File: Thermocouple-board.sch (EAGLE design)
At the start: 69 parts, among them J1 RJ45, J11 1X2-3.5MM, J12 1X2-3.5MM, J13 1X2-3.5MM, J14 1X2-3.5MM, J2 RJ45, J3 1981584-1, SW1 PUSHBUTTON, SW2 PUSHBUTTON, U1 STM32F030K6, U10 MAX31855, U11 MAX31855, U12 MAX31855, U13 MAX31855, U20 EEPROM-I2C, U21 EEPROM-I2C, U30 ST3485, U40 LP298XS

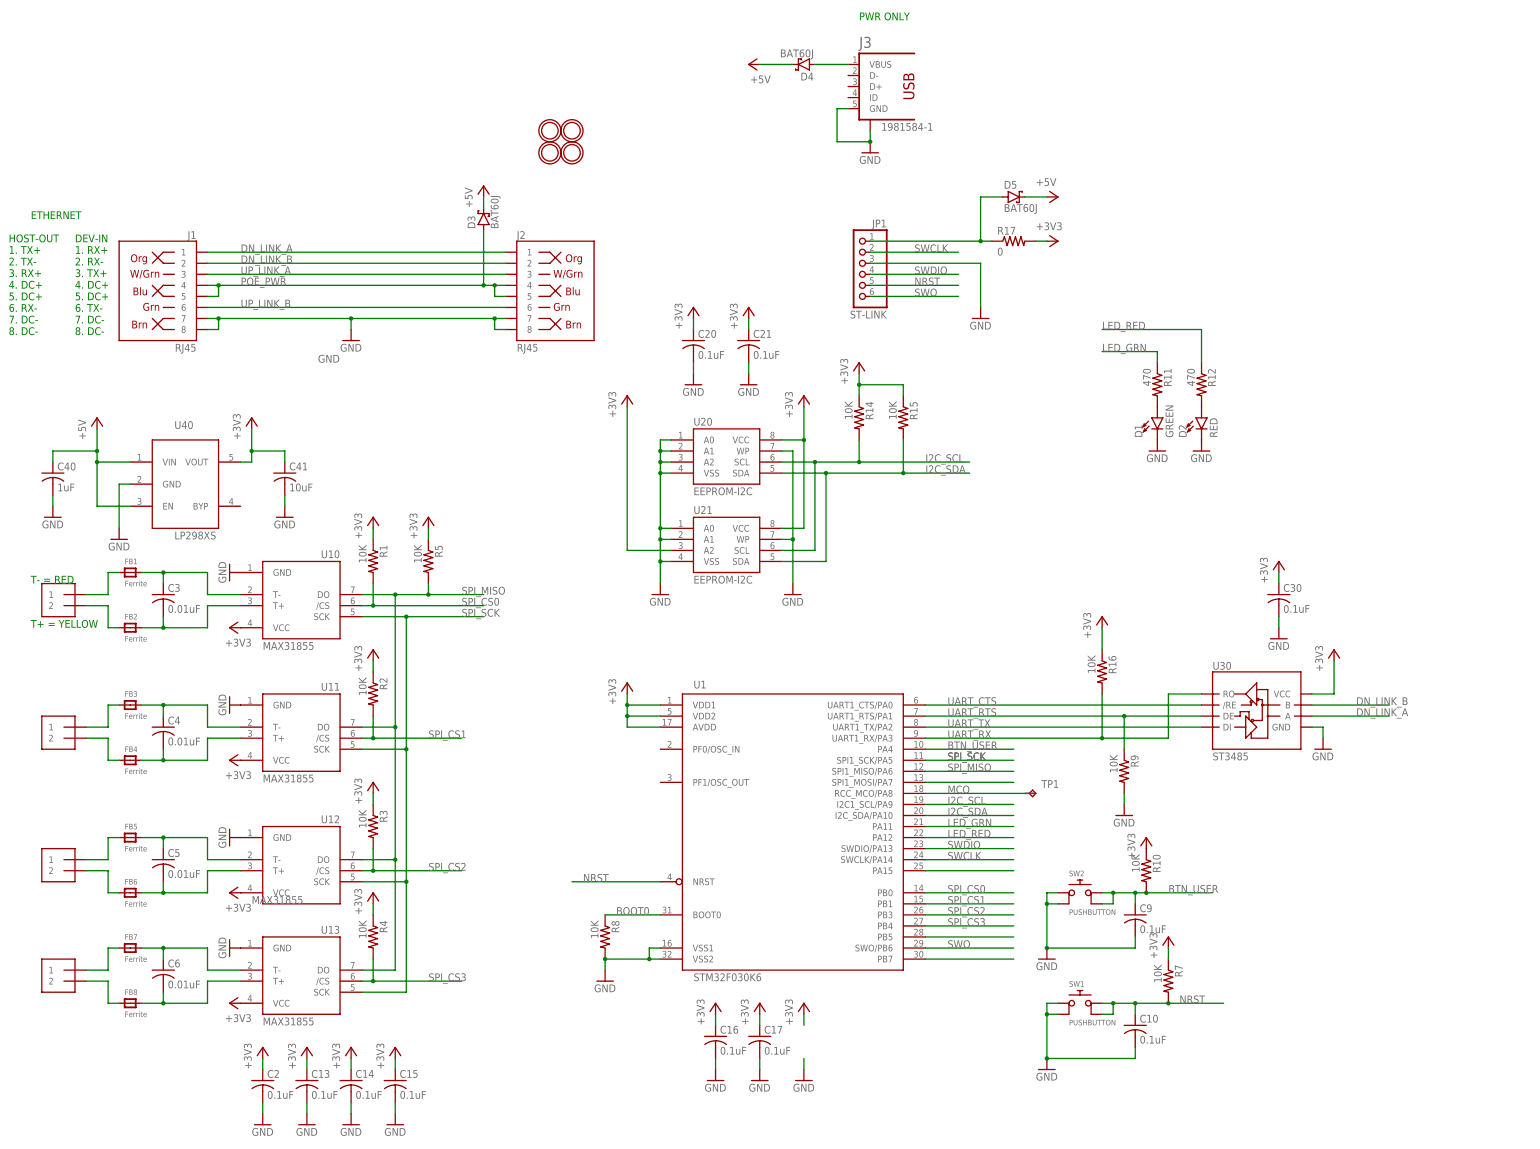
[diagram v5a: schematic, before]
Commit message: Start of move to STM32F042K4 with USB
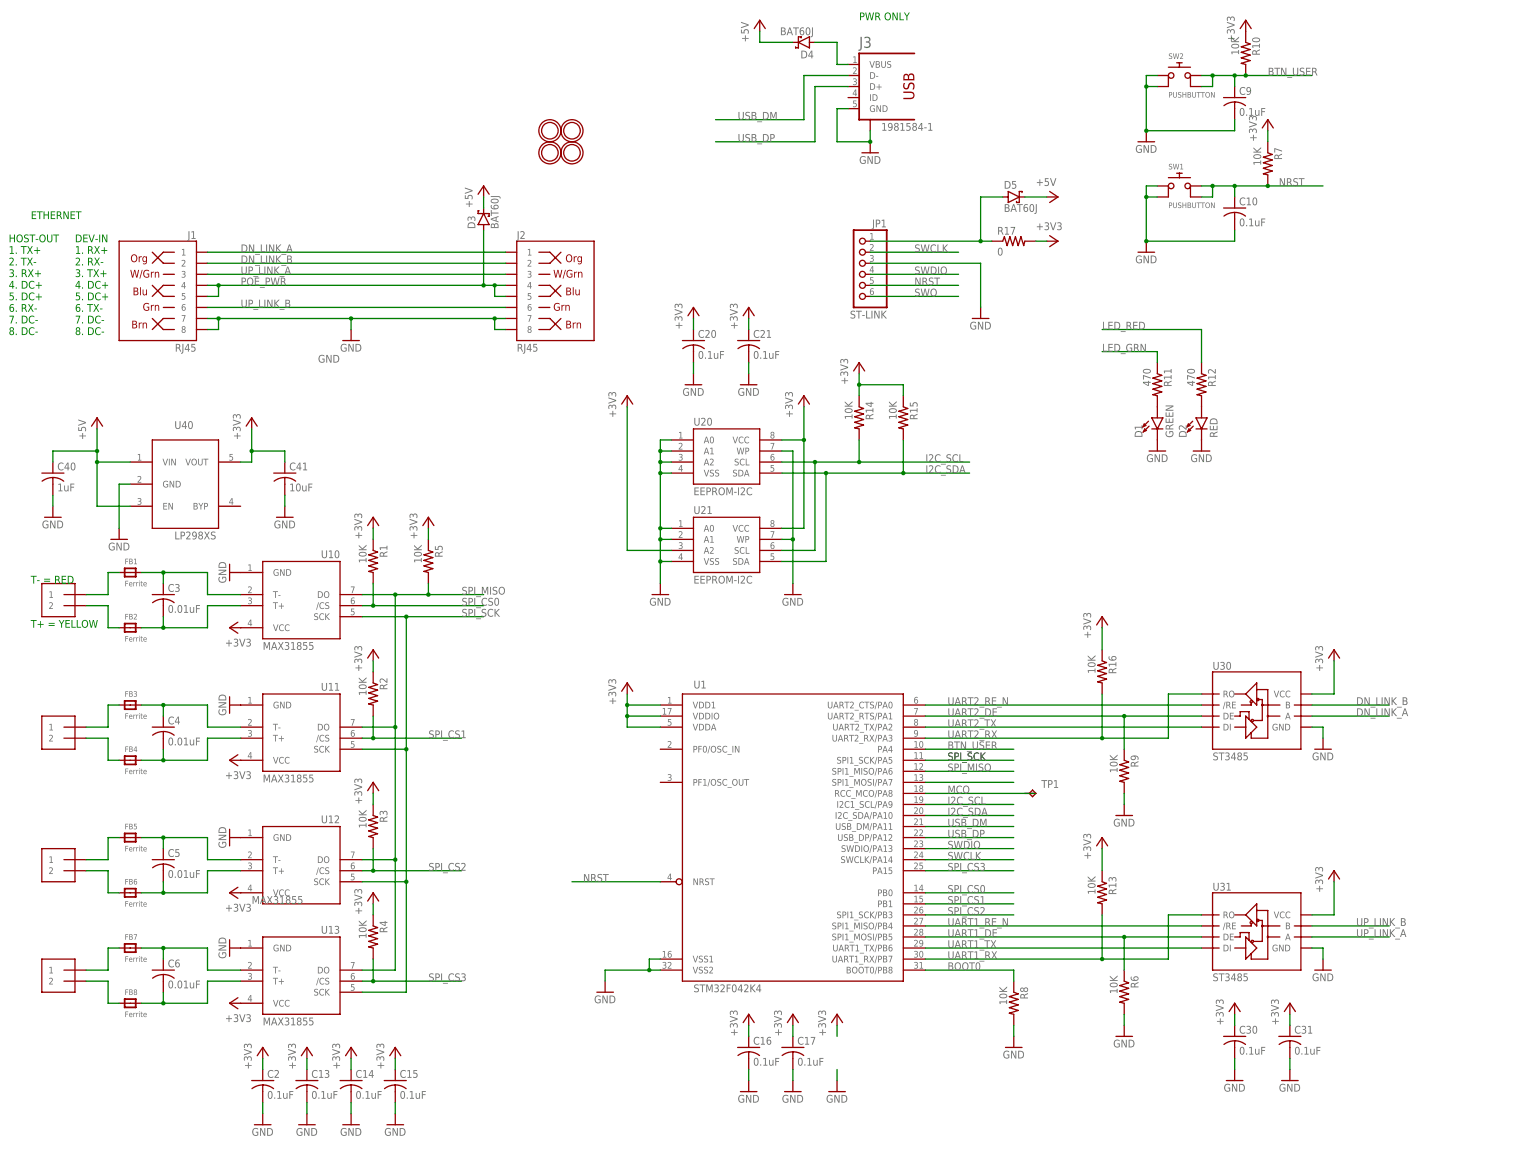
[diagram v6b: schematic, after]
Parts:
- added C31: 0.1uF, adafruit:C-USC0805K
- added R13, R6: 10K, adafruit:R-US_R0805
- added U31: ST3485, SparkFun-IC-Comms:RS485SOIC
- U1: value STM32F030K6 -> STM32F042K4; device Thermocouple-board:STM32F030K6_V01 -> Thermocouple-board:STM32F042K4_V01
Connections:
- removed net N$31: U1.PB5
- removed net N$35: U1.PB7
- removed net N$36: U1.PA15
- removed net UART_CTS: U1.UART1_CTS/PA0, U30./RE
- removed net UART_RTS: R9.1, U1.UART1_RTS/PA1, U30.DE
- removed net UART_RX: R16.2, U1.UART1_RX/PA3, U30.RO
- removed net UART_TX: U1.UART1_TX/PA2, U30.DI
- new net UART1_DE: R6.1, U1.SPI1_MOSI/PB5, U31.DE
- new net UART1_RE_N: U1.SPI1_MISO/PB4, U31./RE
- new net UART1_RX: R13.2, U1.UART1_RX/PB7, U31.RO
- new net UART1_TX: U1.UART1_TX/PB6, U31.DI
- new net UART2_DE: R9.1, U1.UART2_RTS/PA1, U30.DE
- new net UART2_RE_N: U1.UART2_CTS/PA0, U30./RE
- new net UART2_RX: R16.2, U1.UART2_RX/PA3, U30.RO
- new net UART2_TX: U1.UART2_TX/PA2, U30.DI
- new net USB_DM: J3.D-, U1.USB_DM/PA11
- new net USB_DP: J3.D+, U1.USB_DP/PA12
- net +3V3: now also C31.1, R13.1, U1.VDDA, U1.VDDIO, U31.VCC; no longer U1.AVDD, U1.VDD2
- net BOOT0: now also U1.BOOT0/PB8; no longer U1.BOOT0
- net GND: now also C31.2, R6.2, U31.GND
- net LED_GRN: no longer U1.PA11
- net LED_RED: no longer U1.PA12
- net SPI_CS2: now also U1.SPI1_SCK/PB3; no longer U1.PB3
- net SPI_CS3: now also U1.PA15; no longer U1.PB4
- net SWO: no longer U1.SWO/PB6
- net UP_LINK_A: now also U31.A
- net UP_LINK_B: now also U31.B
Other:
- moved on the sheet: C10, C16, C17, C30, C9, D4, R10, R7, R8, SW1, SW2, U1

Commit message: Ripup and start rerouting with USB and Xtal
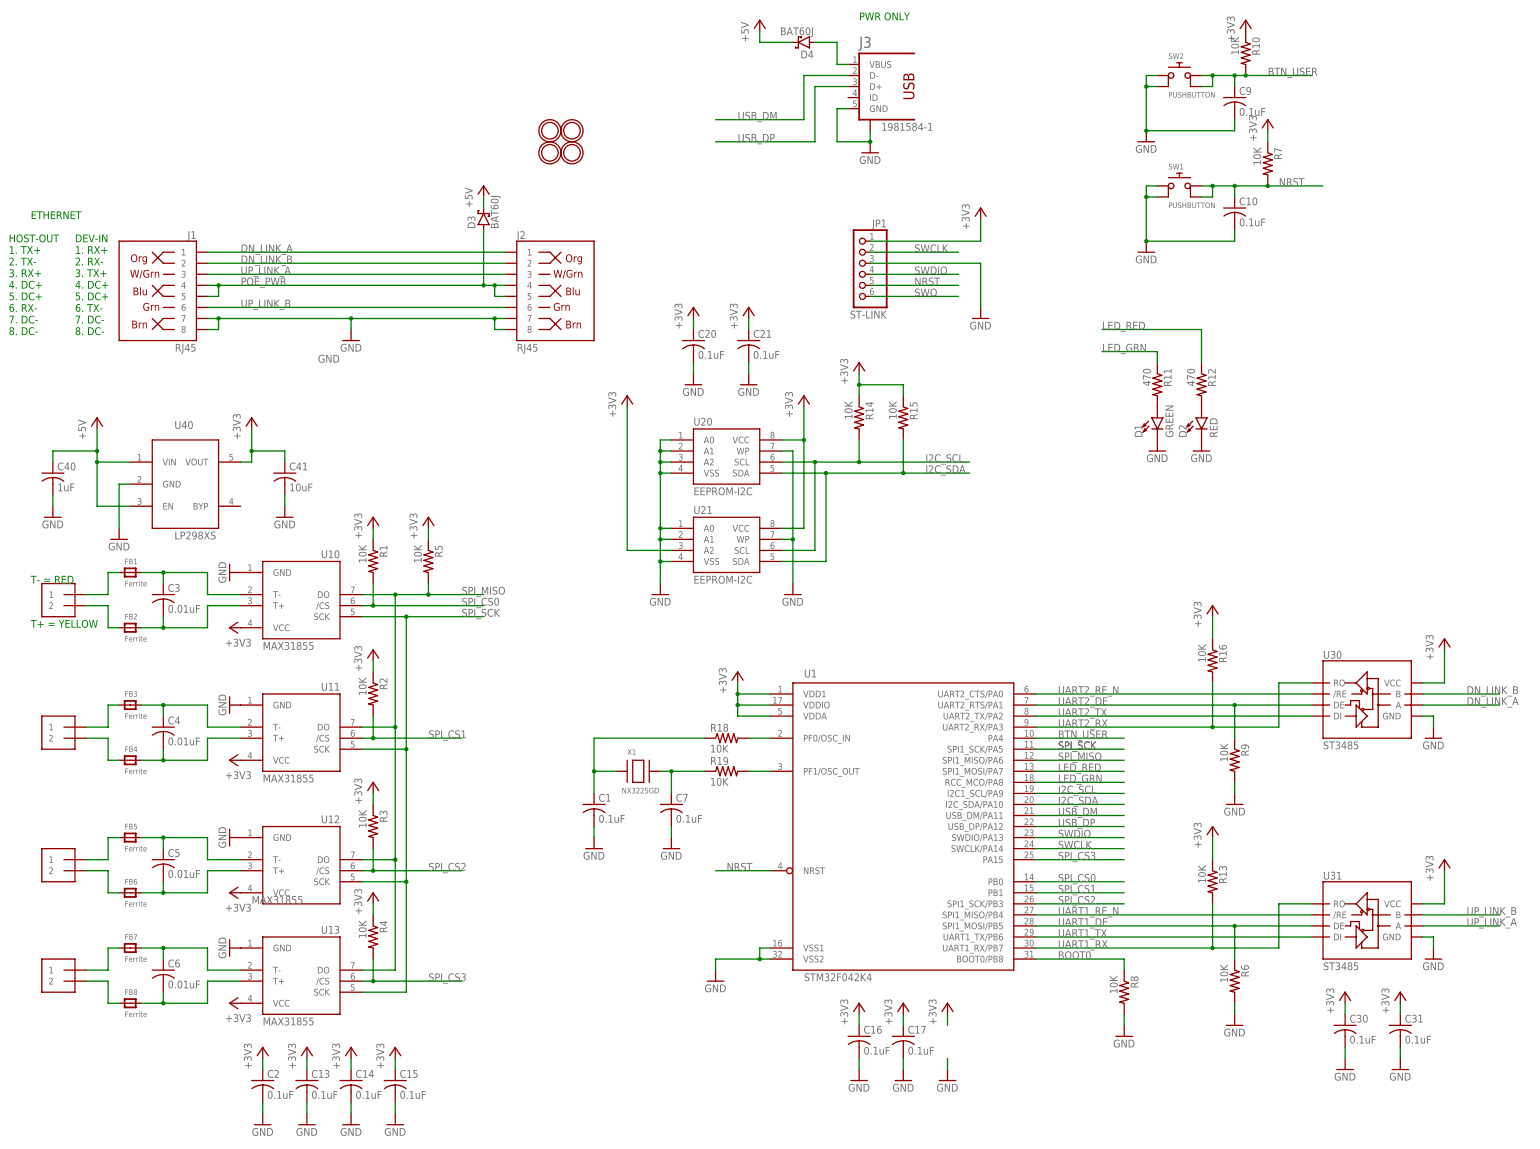
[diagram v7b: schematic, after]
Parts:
- removed D5: BAT60J, diode:BAT60J
- removed R17: 0, adafruit:R-US_R0805
- removed TP1: TPTP08R, testpad:TPTP08R
- added C1, C7: 0.1uF, adafruit:C-USC0805K
- added R18, R19: 10K, adafruit:R-US_R0805
- added X1: NX3225GD, Thermocouple-board:NX3225GD
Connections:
- removed net MCO: TP1.TP, U1.RCC_MCO/PA8
- removed net N$23: D5.A, JP1.1, R17.1
- removed net N$39: U1.SPI1_MOSI/PA7
- new net N$19: C7.1, R19.1, X1.X2
- new net N$2: R18.2, U1.PF0/OSC_IN
- new net N$20: C1.1, R18.1, X1.X1
- new net N$3: R19.2, U1.PF1/OSC_OUT
- net +3V3: now also JP1.1; no longer R17.2
- net +5V: no longer D5.C
- net GND: now also C1.2, C7.2
- net LED_GRN: now also U1.RCC_MCO/PA8
- net LED_RED: now also U1.SPI1_MOSI/PA7
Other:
- moved on the sheet: C16, C17, C30, C31, R13, R16, R6, R8, R9, U1, U30, U31

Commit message: Before replacement of EEPROM
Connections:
- net SPI_CS0 renamed SPI_CS0_N
- net SPI_CS1 renamed SPI_CS1_N
- net SPI_CS2 renamed SPI_CS2_N
- net SPI_CS3 renamed SPI_CS3_N
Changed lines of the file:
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@@
 </variantdefs>
 <classes>
-<class number="0" name="default" width="0" drill="0">
+<class number="0" name="default" width="0.2032" drill="0">
+<clearance class="0" value="0.2032"/>
+</class>
+<class number="1" name="pwr_gnd" width="0.8128" drill="0">
+<clearance class="1" value="0.254"/>
 </class>
 </classes>
@@
 </segment>
 </net>
-<net name="SPI_CS0" class="0">
+<net name="SPI_CS0_N" class="0">
 <segment>
 <pinref part="U10" gate="G$1" pin="/CS"/>
@@
 </segment>
 </net>
-<net name="SPI_CS1" class="0">
+<net name="SPI_CS1_N" class="0">
 <segment>
 <pinref part="U11" gate="G$1" pin="/CS"/>
@@
 </segment>
 </net>
-<net name="SPI_CS2" class="0">
+<net name="SPI_CS2_N" class="0">
 <segment>
 <pinref part="U12" gate="G$1" pin="/CS"/>
@@
 </segment>
 </net>
-<net name="SPI_CS3" class="0">
+<net name="SPI_CS3_N" class="0">
 <segment>
 <pinref part="U13" gate="G$1" pin="/CS"/>
